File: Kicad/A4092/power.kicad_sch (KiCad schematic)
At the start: 35 parts, among them J7 22112042

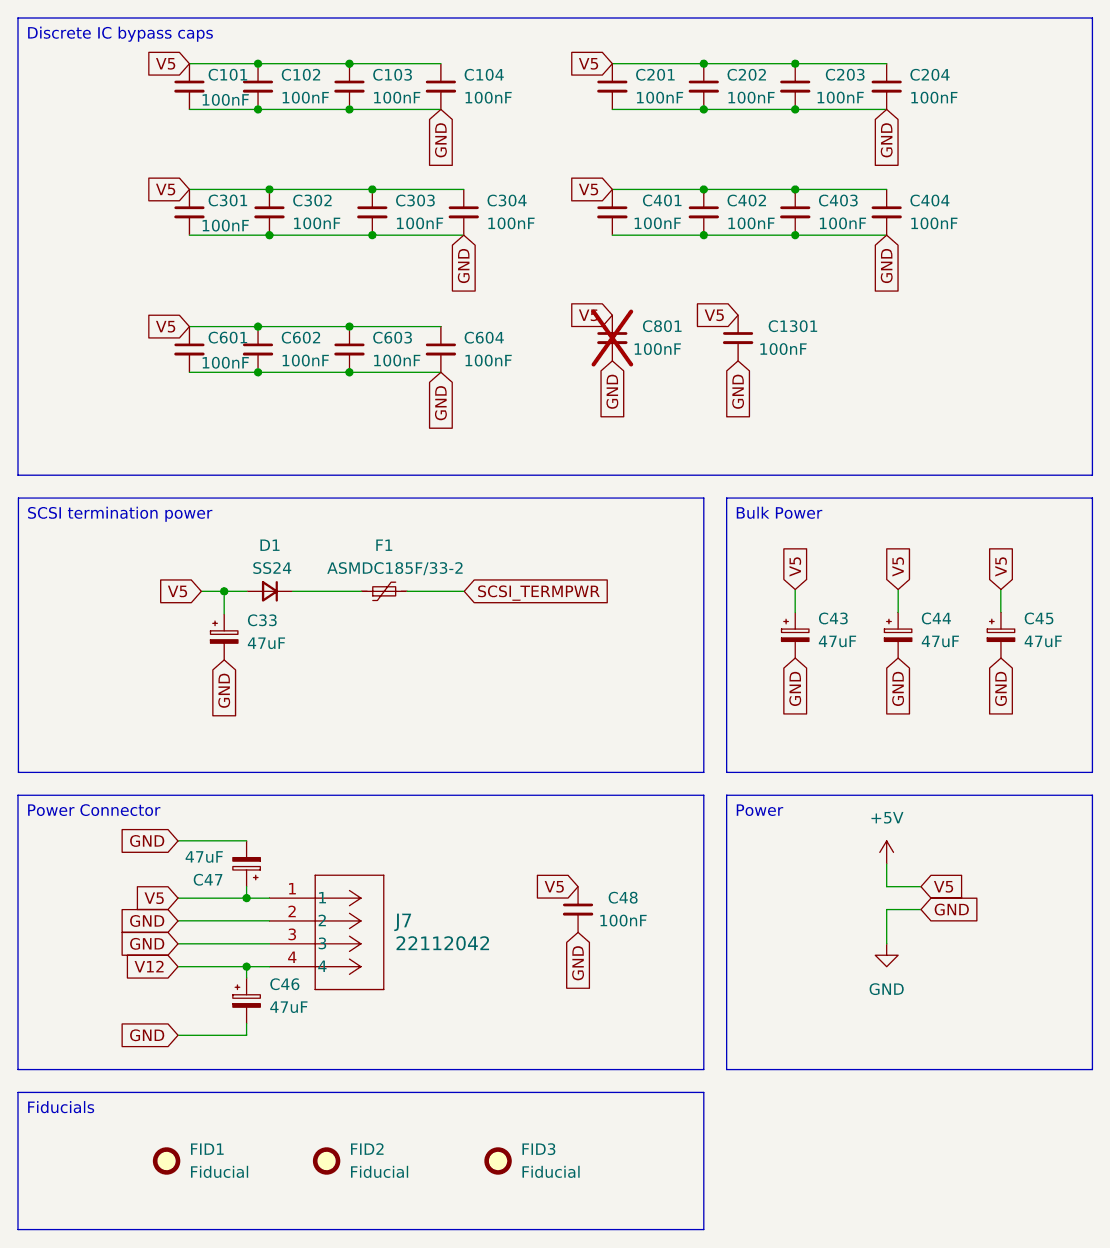
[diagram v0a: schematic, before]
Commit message: A4092 Schematics Revision C
- Power U5 / 74LVC07 from 3.3V rail
- Use ABOEH for 1OEAB on U4 / 74ABT16543
- Add bypass capacitor C501 for U5 / 74LVC07
- Remove EMI filters and capacitors from SCSI lines. They
  are a net negative for signal integrity
- Remove DIP switch circuit as all options are controlled
  by the CPLD / AutoConfig ROM now.
- Remove parallel flash memory, as SPI works reliably and
  is significantly easier to source.
- Remove all ferrite beads from signal lines, as these were
  populated with 0 Ohm resistors in all Proto devices.
- Mark power connector and 12V capacitor as DNP
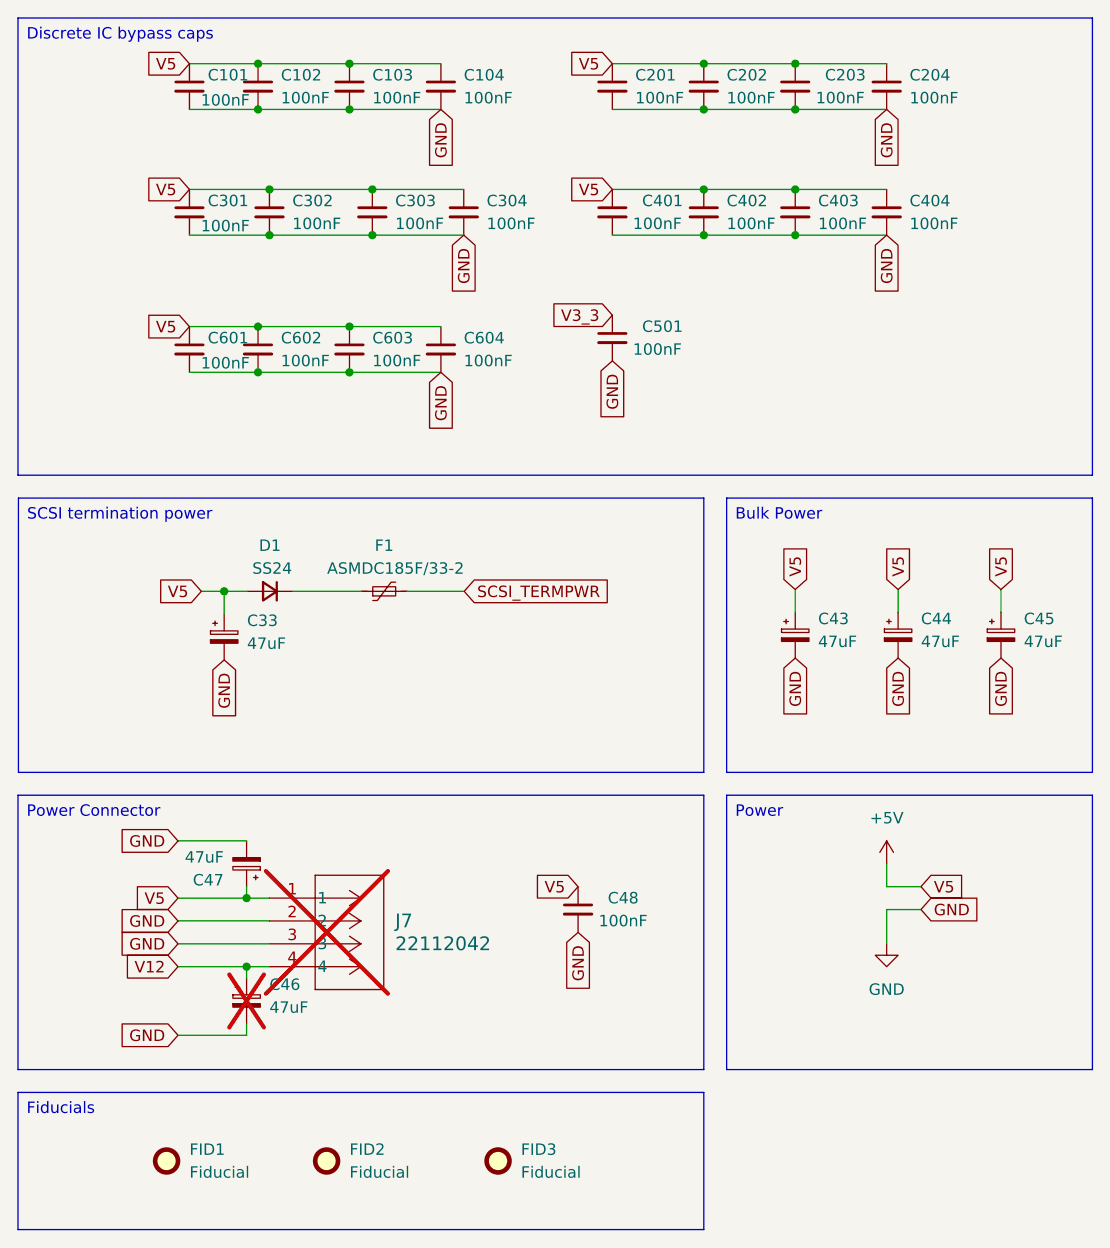
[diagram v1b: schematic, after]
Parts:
- removed C1301: 100nF, Capacitor_SMD:C_0603_1608Metric_Pad1.08x0.95mm_HandSolder, symbol Device:C_Small
- C46, J7: now not fitted
- C501: renamed from C801; now fitted
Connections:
- net +5V: no longer C501.1
- new net V3_3: C501.1
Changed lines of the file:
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@@
 	(title_block
 		(title "A4092")
-		(rev "PROTO0")
+		(date "2026-01-08")
+		(rev "REV C")
 		(company "amiga.technology")
 	)
@@
 		)
 	)
-	(global_label "V5"
-		(shape input)
-		(at 86.36 55.88 180)
-		(fields_autoplaced yes)
-		(effects
-			(font
-				(size 1.27 1.27)
-			)
-			(justify right)
-		)
-		(property "Intersheetrefs" "${INTERSHEET_REFS}"
-			(at 81.0767 55.88 0)
-			(effects
-				(font
-					(size 1.27 1.27)
-				)
-				(justify right)
-				(hide yes)
-			)
-		)
-	)
-	(global_label "GND"
-		(shape input)
-		(at 100.33 60.96 270)
-		(fields_autoplaced yes)
-		(effects
-			(font
-				(size 1.27 1.27)
-			)
-			(justify right)
-		)
-		(property "Intersheetrefs" "${INTERSHEET_REFS}"
-			(at 100.33 67.8157 90)
-			(effects
-				(font
-					(size 1.27 1.27)
-				)
-				(justify right)
-				(hide yes)
-			)
-		)
-	)
 	(global_label "GND"
 		(shape input)
@@
 	(global_label "V5"
 		(shape input)
-		(at 100.33 55.88 180)
-		(fields_autoplaced yes)
-		(effects
-			(font
-				(size 1.27 1.27)
-			)
-			(justify right)
-		)
-		(property "Intersheetrefs" "${INTERSHEET_REFS}"
-			(at 95.0467 55.88 0)
-			(effects
-				(font
-					(size 1.27 1.27)
-				)
-				(justify right)
-				(hide yes)
-			)
-		)
-	)
-	(global_label "V5"
-		(shape input)
 		(at 118.11 86.36 90)
 		(fields_autoplaced yes)
@@
 		)
 	)
+	(global_label "V3_3"
+		(shape input)
+		(at 86.36 55.88 180)
+		(fields_autoplaced yes)
+		(effects
+			(font
+				(size 1.27 1.27)
+			)
+			(justify right)
+		)
+		(property "Intersheetrefs" "${INTERSHEET_REFS}"
+			(at 78.8996 55.88 0)
+			(effects
+				(font
+					(size 1.27 1.27)
+				)
+				(justify right)
+				(hide yes)
+			)
+		)
+	)
 	(global_label "GND"
 		(shape input)
@@
 		(in_bom yes)
 		(on_board yes)
-		(dnp no)
+		(dnp yes)
 		(fields_autoplaced yes)
 		(property "Reference" "C46"
@@
 		(in_bom yes)
 		(on_board yes)
-		(dnp yes)
-		(property "Reference" "C801"
+		(dnp no)
+		(property "Reference" "C501"
 			(at 89.662 57.15 0)
 			(effects
@@
 			(project "A4092"
 				(path "/8f9f4021-47aa-41d9-bea7-f6ccf72098bb/166c366c-e5f9-4398-87d9-75fc4b57be99"
-					(reference "C801")
+					(reference "C501")
 					(unit 1)
 				)
@@
 		(in_bom yes)
 		(on_board yes)
-		(dnp no)
+		(dnp yes)
 		(fields_autoplaced yes)
 		(property "Reference" "J7"
@@
 					(unit 1)
 				)
-			)
-		)
-	)
-	(symbol
-		(lib_id "Device:C_Small")
-		(at 100.33 58.42 0)
-		(unit 1)
-		(exclude_from_sim no)
-		(in_bom yes)
-		(on_board yes)
-		(dnp no)
-		(property "Reference" "C1301"
-			(at 103.632 57.15 0)
-			(effects
-				(font
-					(size 1.27 1.27)
-				)
-				(justify left)
-			)
-		)
-		(property "Value" "100nF"
-			(at 102.616 59.69 0)
-			(effects
-				(font
-					(size 1.27 1.27)
-				)
-				(justify left)
-			)
-		)
-		(property "Footprint" "Capacitor_SMD:C_0603_1608Metric_Pad1.08x0.95mm_HandSolder"
-			(at 100.33 58.42 0)
-			(effects
-				(font
-					(size 1.27 1.27)
-				)
-				(hide yes)
-			)
-		)
-		(property "Datasheet" "~"
-			(at 100.33 58.42 0)
-			(effects
-				(font
-					(size 1.27 1.27)
-				)
-				(hide yes)
-			)
-		)
-		(property "Description" "Unpolarized capacitor, small symbol"
-			(at 100.33 58.42 0)
-			(effects
-				(font
-					(size 1.27 1.27)
-				)
-				(hide yes)
-			)
-		)
-		(property "LCSC Part #" "C14663"
-			(at 100.33 58.42 0)
-			(effects
-				(font
-					(size 1.27 1.27)
-				)
-				(hide yes)
-			)
-		)
-		(pin "2"
-		)
-		(pin "1"
-		)
-		(instances
-			(project "A4092"
-				(path "/8f9f4021-47aa-41d9-bea7-f6ccf72098bb/166c366c-e5f9-4398-87d9-75fc4b57be99"
-					(reference "C1301")
-					(unit 1)
-				)

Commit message: Switch to Littelfuse SMDC185F/33-2
Previously used JDTfuse ASMD2920-185 but I have 200
pieces of Littelfuse SMDC185F/33-2 consigned.
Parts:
- F1: LCSC Part # C135379 -> C3761950
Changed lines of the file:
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@@
 			)
 		)
-		(property "LCSC Part #" "C135379"
+		(property "LCSC Part #" "C3761950"
 			(at 61.0106 86.5643 90)
 			(effects
